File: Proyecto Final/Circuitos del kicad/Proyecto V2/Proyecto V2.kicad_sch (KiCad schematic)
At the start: 44 parts, among them J1 12v, J2 I2C + LCD, J3 DS1307, Q1 PN2222A, Q2 PN2222A, Q3 PN2222A, SW1 SW_Push, SW2 SW_Push, SW3 SW_Push, SW4 SW_Push, U1 LM7805, U3 ATmega328P-P, Y1 16MHz

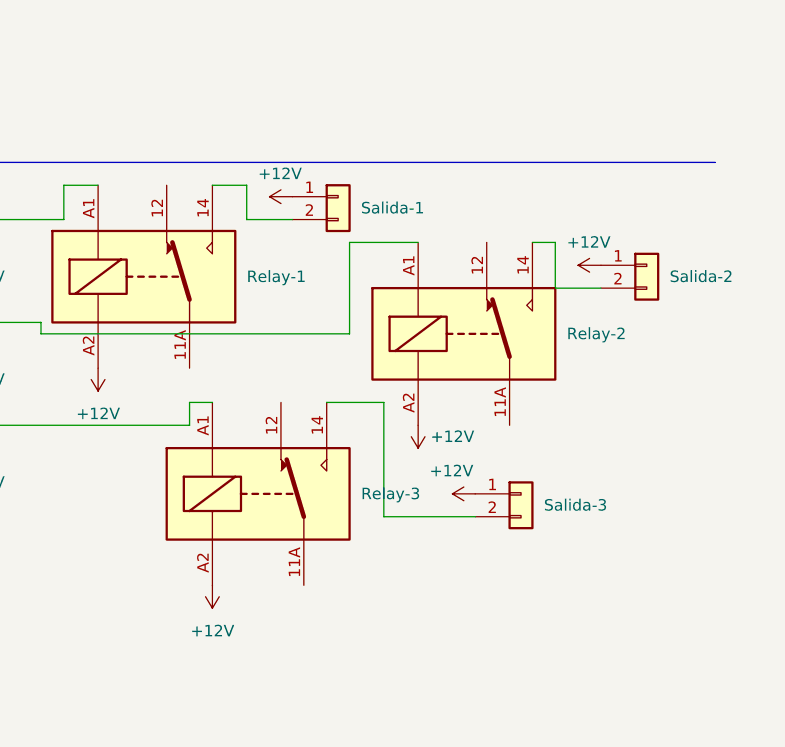
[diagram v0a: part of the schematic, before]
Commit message: Agregado pines IDC, arreglo rele
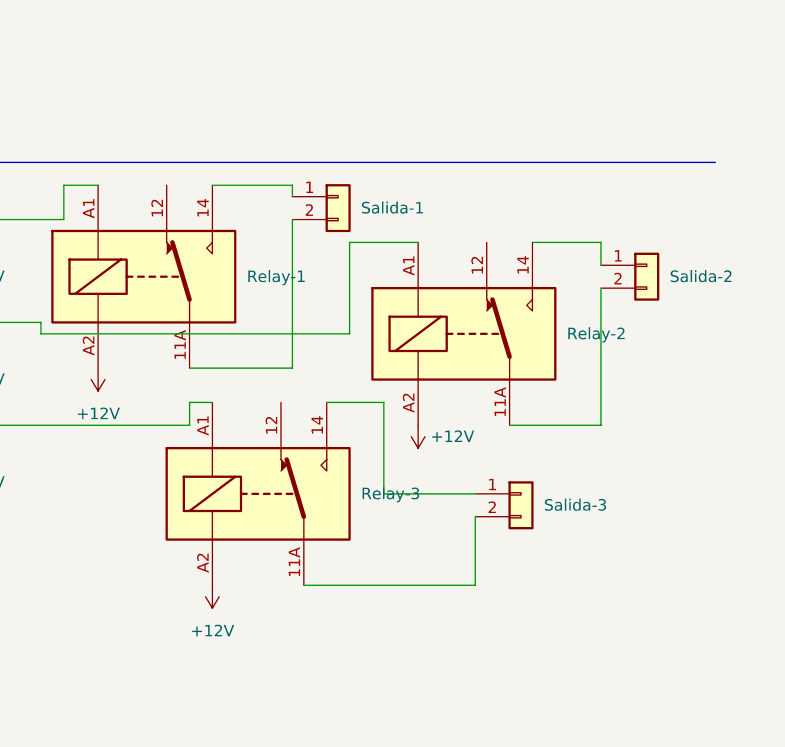
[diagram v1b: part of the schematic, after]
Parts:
- Encoder/puls-arduino1, Encoder/puls1: footprint Connector_PinHeader_2.54mm:PinHeader_2x06_P2.54mm_Vertical -> Connector_IDC:IDC-Header_2x06_P2.54mm_Vertical
- RELAY1, RELAY2: footprint Connector_PinHeader_2.54mm:PinHeader_1x05_P2.54mm_Vertical -> Connector_IDC:IDC-Header_2x05_P2.54mm_Vertical
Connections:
- net +12V: no longer Salida-1.1 (Pin_1), Salida-2.1 (Pin_1), Salida-3.1 (Pin_1)
- net at Relay-1.11A, Relay-1.11B: now also Salida-1.2 (Pin_2)
- net at Relay-1.14: now also Salida-1.1 (Pin_1); no longer Salida-1.2 (Pin_2)
- net at Relay-3.14: now also Salida-3.1 (Pin_1); no longer Salida-3.2 (Pin_2)
- net at Relay-2.14: now also Salida-2.1 (Pin_1); no longer Salida-2.2 (Pin_2)
- net at Relay-2.11A, Relay-2.11B: now also Salida-2.2 (Pin_2)
- net at Relay-3.11A, Relay-3.11B: now also Salida-3.2 (Pin_2)

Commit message: Update PCB
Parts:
- removed RELAY1, RELAY2: Conn_01x05, Connector_IDC:IDC-Header_2x05_P2.54mm_Vertical, symbol Connector_Generic:Conn_01x05
- added Relay1: Conn_02x05_Top_Bottom, Connector_IDC:IDC-Header_2x05_P2.54mm_Vertical, symbol Connector_Generic:Conn_02x05_Top_Bottom
- added Relay2: Relay2, Connector_IDC:IDC-Header_2x05_P2.54mm_Vertical, symbol Connector_Generic:Conn_02x05_Top_Bottom
- Encoder1: footprint Connector_PinSocket_2.54mm:PinSocket_1x05_P2.54mm_Vertical -> Connector_PinHeader_2.54mm:PinHeader_1x05_P2.54mm_Vertical
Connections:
- net +12V: now also D1.2 (A), D2.2 (A), D3.2 (A), Relay1.5 (Pin_5), Relay2.1 (Pin_1); no longer D1.1 (K), D2.1 (K), D3.1 (K), Relay-1.A2, Relay-2.A2, Relay-3.A2
- net GND: now also Relay-1.A2, Relay-2.A2, Relay-3.A2, Relay1.1 (Pin_1), Relay2.5 (Pin_5)
- net at Q3.3 (C), Relay-1.A1: now also D1.1 (K); no longer D1.2 (A)
- net at Q1.3 (C), Relay-3.A1: now also D3.1 (K); no longer D3.2 (A)
- net at R3.2: now also Relay2.2 (Pin_2)
- net at Q2.3 (C), Relay-2.A1: now also D2.1 (K); no longer D2.2 (A)
- net at R2.2: now also Relay2.3 (Pin_3)
- net at R4.2: now also Relay2.4 (Pin_4)
- net at U3.17 (PB3): now also Relay1.4 (Pin_4)
- net at U3.18 (PB4): now also Relay1.3 (Pin_3)
- net at U3.19 (PB5): now also Relay1.2 (Pin_2)
- no-connect marks 34 -> 44
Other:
- moved on the sheet: D1, D2, D3

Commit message: Cambios plaqueta
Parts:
- removed DS18B20: Conn_01x03, Connector_PinHeader_2.54mm:PinHeader_1x03_P2.54mm_Vertical, symbol Connector_Generic:Conn_01x03
- removed J2: I2C + LCD, Connector_PinSocket_2.54mm:PinSocket_1x04_P2.54mm_Vertical, symbol Connector_Generic:Conn_01x04
- removed J3: DS1307, Connector_PinSocket_2.54mm:PinSocket_1x04_P2.54mm_Vertical, symbol Connector_Generic:Conn_01x04
- removed Lvl_sens1: lvl_sens, Connector_PinSocket_2.54mm:PinSocket_1x03_P2.54mm_Vertical, symbol Connector_Generic:Conn_01x03
- removed Relay1: Conn_02x05_Top_Bottom, Connector_IDC:IDC-Header_2x05_P2.54mm_Vertical, symbol Connector_Generic:Conn_02x05_Top_Bottom
- removed Relay2: Relay2, Connector_IDC:IDC-Header_2x05_P2.54mm_Vertical, symbol Connector_Generic:Conn_02x05_Top_Bottom
- added DS18B20+LVL_SENS1: Conn_02x03_Odd_Even, Connector_IDC:IDC-Header_2x03_P2.54mm_Vertical, symbol Connector_Generic:Conn_02x03_Odd_Even
- added RTC+LCD1: Conn_02x04_Odd_Even, Connector_PinHeader_2.54mm:PinHeader_2x04_P2.54mm_Vertical, symbol Connector_Generic:Conn_02x04_Odd_Even
- added Relay1, Relay2: Conn_02x05_Odd_Even, Connector_IDC:IDC-Header_2x05_P2.54mm_Vertical, symbol Connector_Generic:Conn_02x05_Odd_Even
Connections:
- net +12V: now also Relay1.2 (Pin_2), Relay2.10 (Pin_10)
- net +5V: now also R1.2, DS18B20+LVL_SENS1.5 (Pin_5), DS18B20+LVL_SENS1.6 (Pin_6), RTC+LCD1.5 (Pin_5), RTC+LCD1.6 (Pin_6); no longer R1.1
- net GND: now also DS18B20+LVL_SENS1.1 (Pin_1), DS18B20+LVL_SENS1.2 (Pin_2), RTC+LCD1.7 (Pin_7), RTC+LCD1.8 (Pin_8), Relay1.10 (Pin_10), Relay2.2 (Pin_2)
- net at Encoder/puls-arduino1.10 (Pin_10): now also U3.13 (PD7)
- net at Encoder/puls-arduino1.3 (Pin_3): now also U3.4 (PD2); no longer U3.6 (PD4)
- net at Encoder/puls-arduino1.4 (Pin_4): now also U3.6 (PD4); no longer U3.4 (PD2)
- net at Encoder/puls-arduino1.5 (Pin_5): now also U3.5 (PD3); no longer U3.11 (PD5)
- net at Encoder/puls-arduino1.6 (Pin_6): now also U3.11 (PD5); no longer U3.5 (PD3)
- net at Encoder/puls-arduino1.7 (Pin_7): now also U3.23 (PC0); no longer U3.12 (PD6)
- net at Encoder/puls-arduino1.8 (Pin_8): now also U3.12 (PD6); no longer U3.23 (PC0)
- net at Encoder/puls-arduino1.9 (Pin_9): no longer U3.13 (PD7)
- net at R3.2: now also Relay2.4 (Pin_4)
- net at R2.2: now also Relay2.8 (Pin_8)
- net at U3.28 (PC5): now also RTC+LCD1.1 (Pin_1), RTC+LCD1.2 (Pin_2)
- net at U3.27 (PC4): now also RTC+LCD1.3 (Pin_3), RTC+LCD1.4 (Pin_4)
- net at R4.2: now also Relay2.6 (Pin_6)
- net at U3.19 (PB5): now also Relay1.4 (Pin_4)
- net at U3.18 (PB4): now also Relay1.6 (Pin_6)
- net at U3.17 (PB3): now also Relay1.8 (Pin_8)
- net at U3.26 (PC3): now also DS18B20+LVL_SENS1.4 (Pin_4)
- net at U3.15 (PB1): no longer R1.2
- net at U3.24 (PC1): now also R1.1, DS18B20+LVL_SENS1.3 (Pin_3)
- no-connect marks 44 -> 46

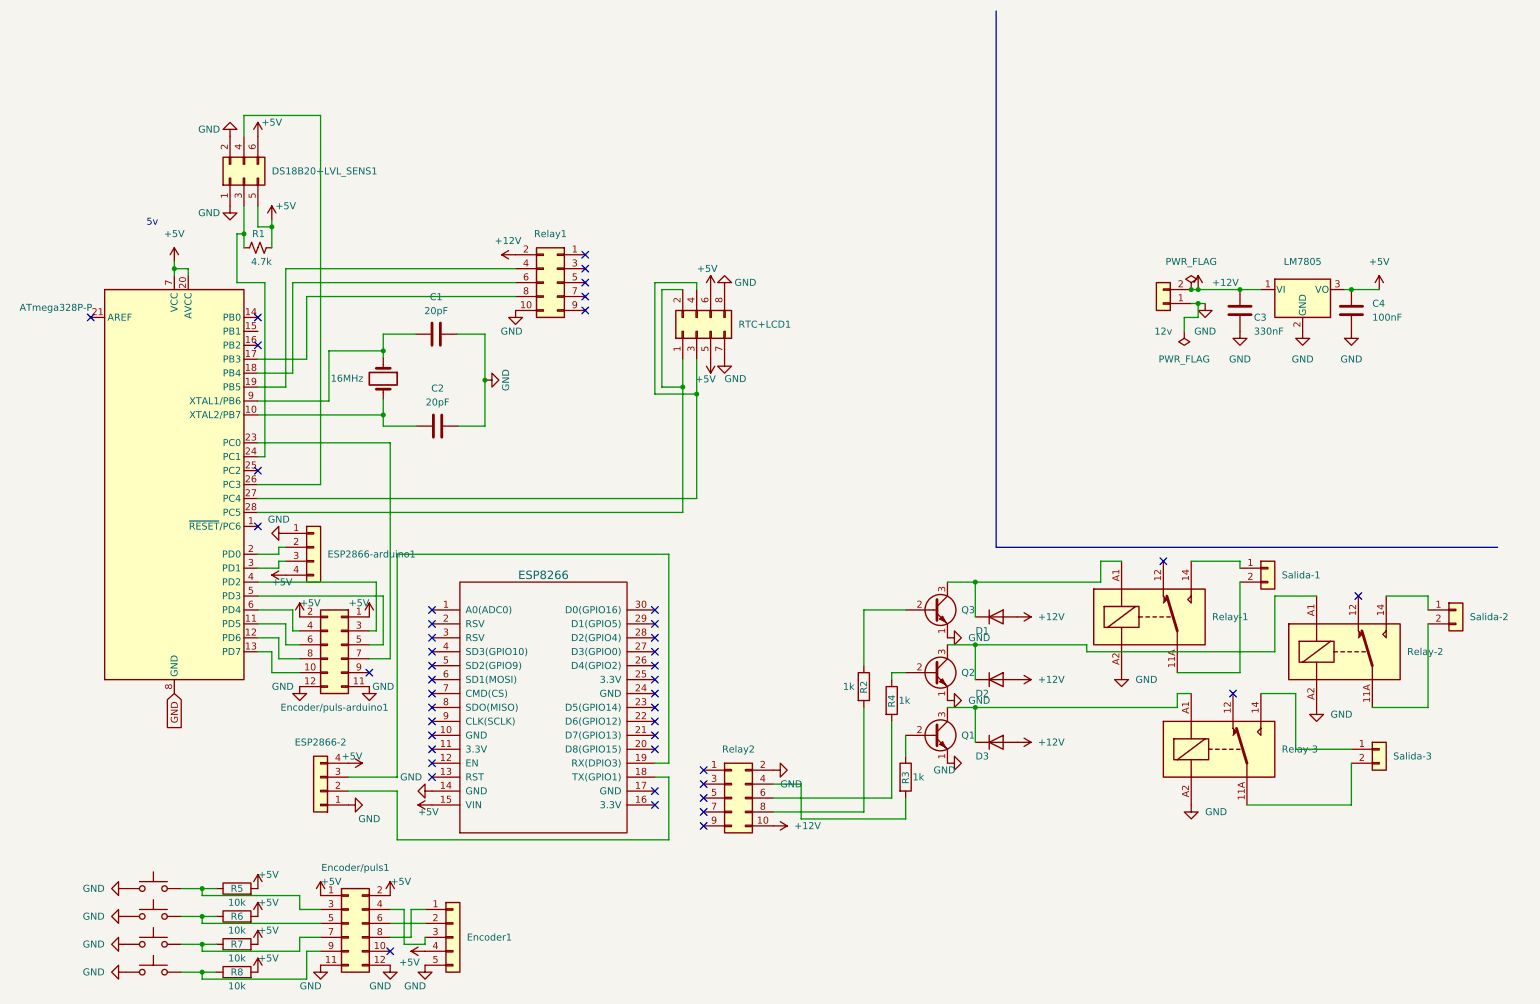
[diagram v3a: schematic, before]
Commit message: Cree libs para el kicad y agregue borneras de sensores
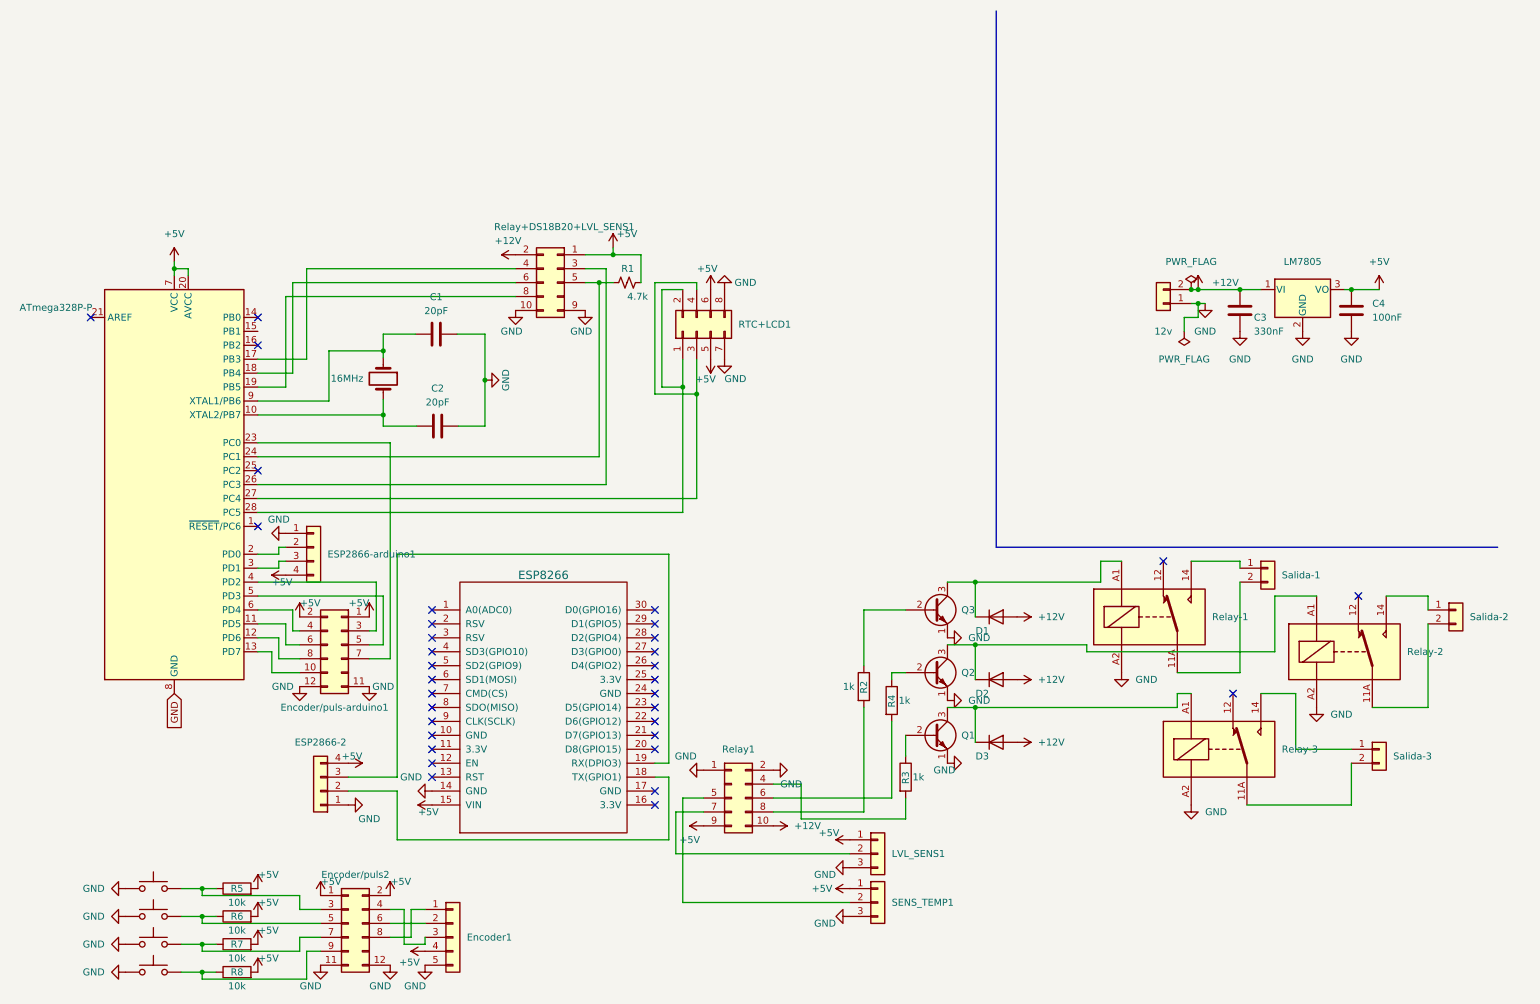
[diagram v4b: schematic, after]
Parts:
- removed DS18B20+LVL_SENS1: Conn_02x03_Odd_Even, Connector_IDC:IDC-Header_2x03_P2.54mm_Vertical, symbol Connector_Generic:Conn_02x03_Odd_Even
- removed Encoder/puls-arduino1, Encoder/puls1: Conn_02x06_Odd_Even, Connector_IDC:IDC-Header_2x06_P2.54mm_Vertical, symbol Connector_Generic:Conn_02x06_Odd_Even
- removed Relay1, Relay2: Conn_02x05_Odd_Even, Connector_IDC:IDC-Header_2x05_P2.54mm_Vertical, symbol Connector_Generic:Conn_02x05_Odd_Even
- added Encoder/puls-arduino1: Conn_02x06_Odd_Even, ENCODER+PULS:ENCODER+PULS_arduino, symbol ENCODER+PULS_arduino:Conn_02x06_Odd_Even
- added Encoder/puls2: Conn_02x06_Odd_Even, ENCODER+PULS:ENCODER+PULS, symbol ENCODER+PULS:Conn_02x06_Odd_Even
- added LVL_SENS1, SENS_TEMP1: Conn_01x03, TerminalBlock:TerminalBlock_bornier-3_P5.08mm, symbol Connector_Generic:Conn_01x03
- added Relay+DS18B20+LVL_SENS1: Conn_02x05_Odd_Even_1, RELAY+DS18B20+LVLSENS:RELAY+DS18B20+LVLSENS, symbol RELAY+DS18B20+LVLSENS:Conn_02x05_Odd_Even_1
- added Relay1: Conn_02x05_Odd_Even, RELAY+DS18B20+LVLSENS:ENCODER+PULS_PLACA_SALIDAS, symbol RELAY+DS18B20+LVLSENS_PLACA_SALIDAS:Conn_02x05_Odd_Even
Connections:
- net +12V: now also Relay+DS18B20+LVL_SENS1.2 (Pin_2), Relay1.10 (Pin_10)
- net +5V: now also Encoder/puls-arduino1.1 (Pin_1), Encoder/puls-arduino1.2 (Pin_2), Encoder/puls2.1 (Pin_1), Encoder/puls2.2 (Pin_2), LVL_SENS1.1 (Pin_1), Relay+DS18B20+LVL_SENS1.1 (Pin_1), Relay1.9 (Pin_9), SENS_TEMP1.1 (Pin_1)
- net GND: now also Encoder/puls-arduino1.11 (Pin_11), Encoder/puls-arduino1.12 (Pin_12), Encoder/puls2.11 (Pin_11), Encoder/puls2.12 (Pin_12), LVL_SENS1.3 (Pin_3), Relay+DS18B20+LVL_SENS1.10 (Pin_10), Relay+DS18B20+LVL_SENS1.9 (Pin_9), Relay1.1 (Pin_1), Relay1.2 (Pin_2), SENS_TEMP1.3 (Pin_3)
- net at R5.1, SW4.2: now also Encoder/puls2.3 (Pin_3)
- net at Encoder1.3 (Pin_3): now also Encoder/puls2.4 (Pin_4)
- net at R6.1, SW3.2: now also Encoder/puls2.5 (Pin_5)
- net at Encoder1.2 (Pin_2): now also Encoder/puls2.6 (Pin_6)
- net at R7.1, SW2.2: now also Encoder/puls2.7 (Pin_7)
- net at Encoder1.1 (Pin_1): now also Encoder/puls2.8 (Pin_8)
- net at R8.1, SW1.2: now also Encoder/puls2.9 (Pin_9)
- net at U3.13 (PD7): now also Encoder/puls-arduino1.10 (Pin_10)
- net at U3.4 (PD2): now also Encoder/puls-arduino1.3 (Pin_3)
- net at U3.6 (PD4): now also Encoder/puls-arduino1.4 (Pin_4)
- net at U3.5 (PD3): now also Encoder/puls-arduino1.5 (Pin_5)
- net at U3.11 (PD5): now also Encoder/puls-arduino1.6 (Pin_6)
- net at U3.23 (PC0): now also Encoder/puls-arduino1.7 (Pin_7)
- net at U3.12 (PD6): now also Encoder/puls-arduino1.8 (Pin_8)
- net at R3.2: now also Relay1.4 (Pin_4)
- net at R2.2: now also Relay1.8 (Pin_8)
- net at U3.19 (PB5): now also Relay+DS18B20+LVL_SENS1.8 (Pin_8)
- net at U3.18 (PB4): now also Relay+DS18B20+LVL_SENS1.6 (Pin_6)
- net at U3.17 (PB3): now also Relay+DS18B20+LVL_SENS1.4 (Pin_4)
- net at R1.1, U3.24 (PC1): now also Relay+DS18B20+LVL_SENS1.5 (Pin_5)
- net at U3.26 (PC3): now also Relay+DS18B20+LVL_SENS1.3 (Pin_3)
- net at R4.2: now also Relay1.6 (Pin_6)
- new net: Relay1.5 (Pin_5), SENS_TEMP1.2 (Pin_2)
- new net: LVL_SENS1.2 (Pin_2), Relay1.7 (Pin_7)
- no-connect marks 46 -> 34
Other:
- note removed: "5v"

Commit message: Cambios plaqueta
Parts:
- R2, R3, R4: value 1k -> 4k7
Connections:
- net +12V: now also D1.1 (K), D2.1 (K), D3.1 (K), Relay-1.A1, Relay-2.A1, Relay-3.A1; no longer D1.2 (A), D2.2 (A), D3.2 (A)
- net GND: no longer Relay-1.A2, Relay-2.A2, Relay-3.A2
- net at ESP8266.18 (TX(GPIO1)): now also ESP2866-2.3 (Pin_3); no longer ESP2866-2.2 (Pin_2)
- net at ESP8266.19 (RX(DPIO3)): now also ESP2866-2.2 (Pin_2); no longer ESP2866-2.3 (Pin_3)
- net at U3.4 (PD2): now also Encoder/puls-arduino1.5 (Pin_5); no longer Encoder/puls-arduino1.3 (Pin_3)
- net at U3.5 (PD3): now also Encoder/puls-arduino1.3 (Pin_3); no longer Encoder/puls-arduino1.5 (Pin_5)
- new net: D1.2 (A), Q3.3 (C), Relay-1.A2
- new net: D3.2 (A), Q1.3 (C), Relay-3.A2
- new net: D2.2 (A), Q2.3 (C), Relay-2.A2
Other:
- moved on the sheet: C3, C4, D2, D3, Q1, Q2, Q3, R2, R4, Relay-1, Relay-2, Relay-3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
